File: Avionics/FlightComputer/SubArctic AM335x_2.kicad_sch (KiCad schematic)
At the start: 0 parts

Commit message: Ian Goldberg - Finished sheet no. 1 of the beagleboard and am on to sheet no. 2
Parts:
- added C34: 100uF,10V, symbol Device:C
- added C35, C36: 100nF,16V, symbol Device:C
- added FB7: 150R,800mA, symbol Device:L
- added R37: 0R,5%, symbol Device:R
- added R52, R53: 10K,1%, symbol Device:R
- added U5: ~, symbol SubArctic AM335x:TPS2051BDGNR
- added U6, U8: ~, symbol SubArctic AM335x:TPD4S012DRYR
- added U7: ~, symbol SubArctic AM335x:UB11123-4H9-4F
- added U9: ~, symbol SubArctic AM335x:UX60SC-MB-5ST
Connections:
- new net: U8. (VBUS), U9. (VB) (x3)
- new net: C35.1, FB7.1, R37.2, U5. (PAD), U6. (VBUS)
- new net: FB7.2, U7. (VBUS)
- new net: R53.1, U5. (PAD)
- new net: U6. (VBUS), U7. (VBUS) (x2)
- new net DGND: C34.2, C35.2, C36.2, R53.2, U5. (PAD), U6. (VBUS), U7. (VBUS), U8. (VBUS), U9. (VB)
- new net GNDPWR: U7. (VBUS), U9. (VB)
- new net SYS_5V: C34.1, U5. (PAD)
- new net USB1_OCn: R52.2, U5. (PAD)
- new net USB_DC: C36.1, U8. (VBUS), U9. (VB)
- new net VDD_3V3A: R52.1
- no-connect marks 0 -> 3

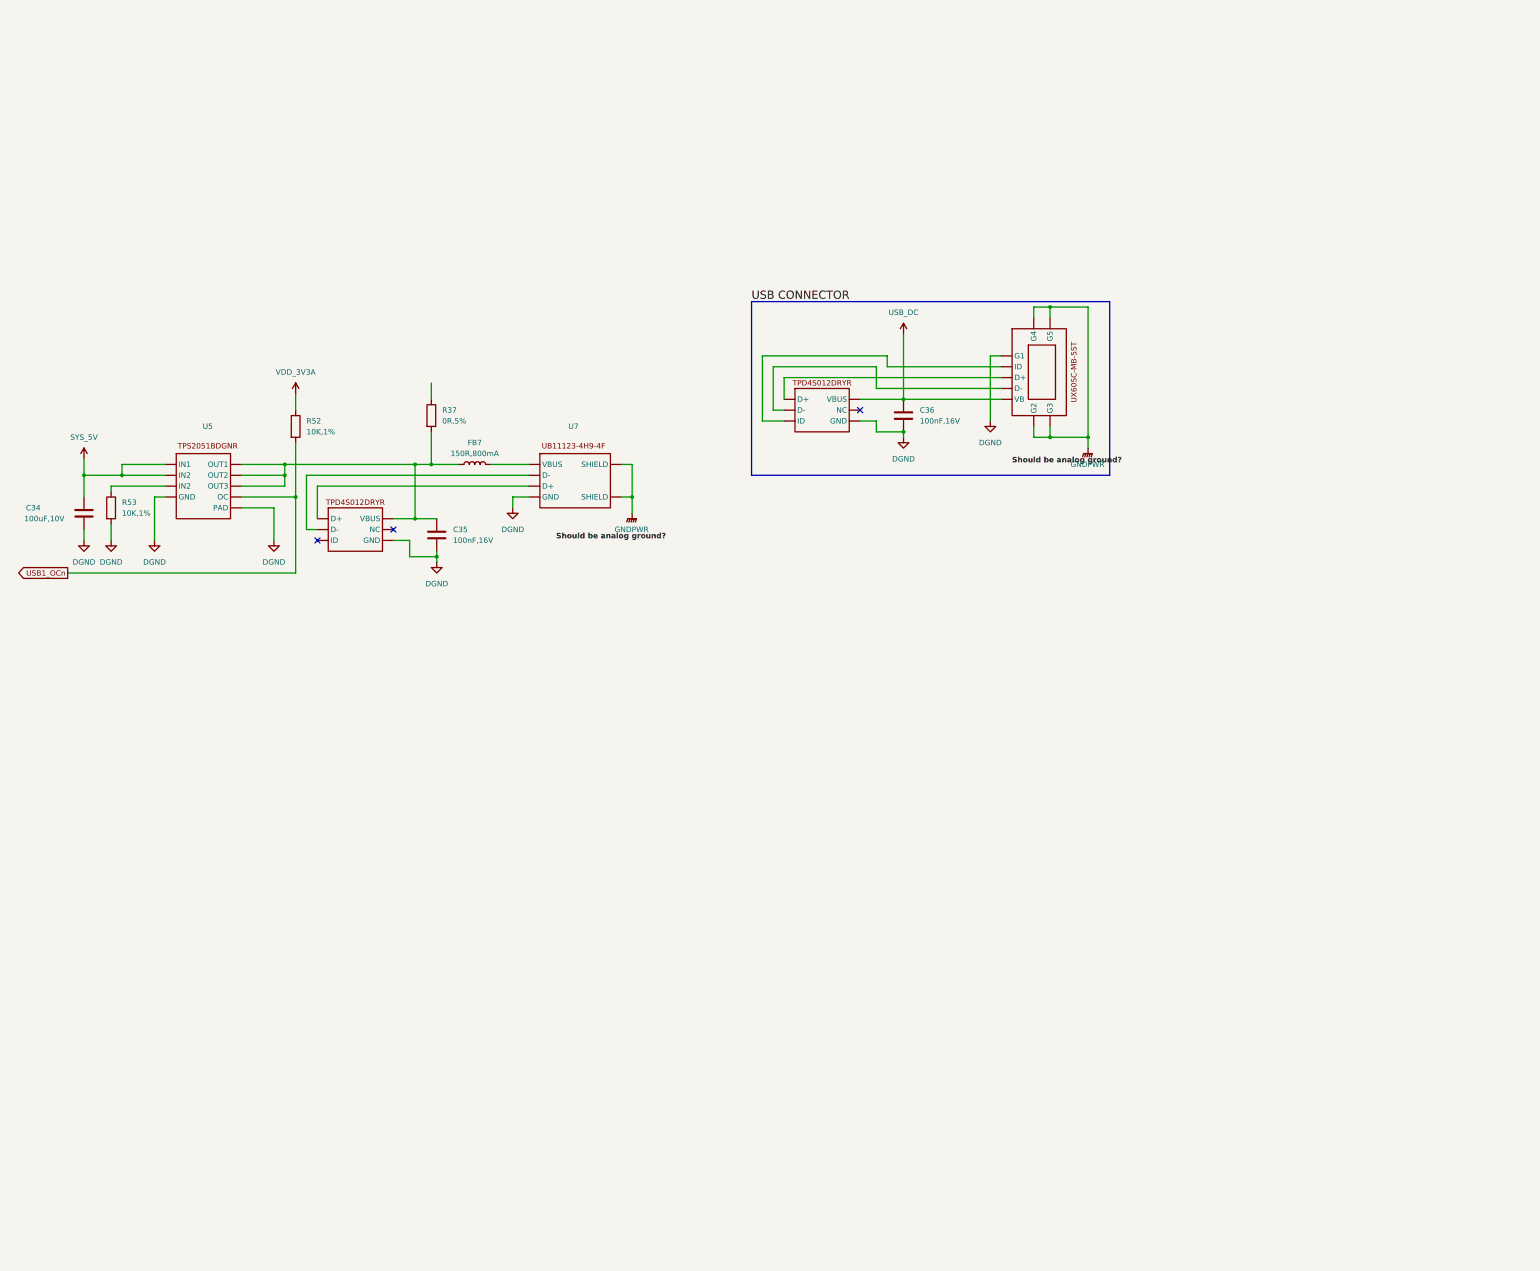
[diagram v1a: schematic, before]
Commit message: Ian Goldberg - Finished the second pin diagram for the SubArctic AM335x chip - only one more to go after this one.
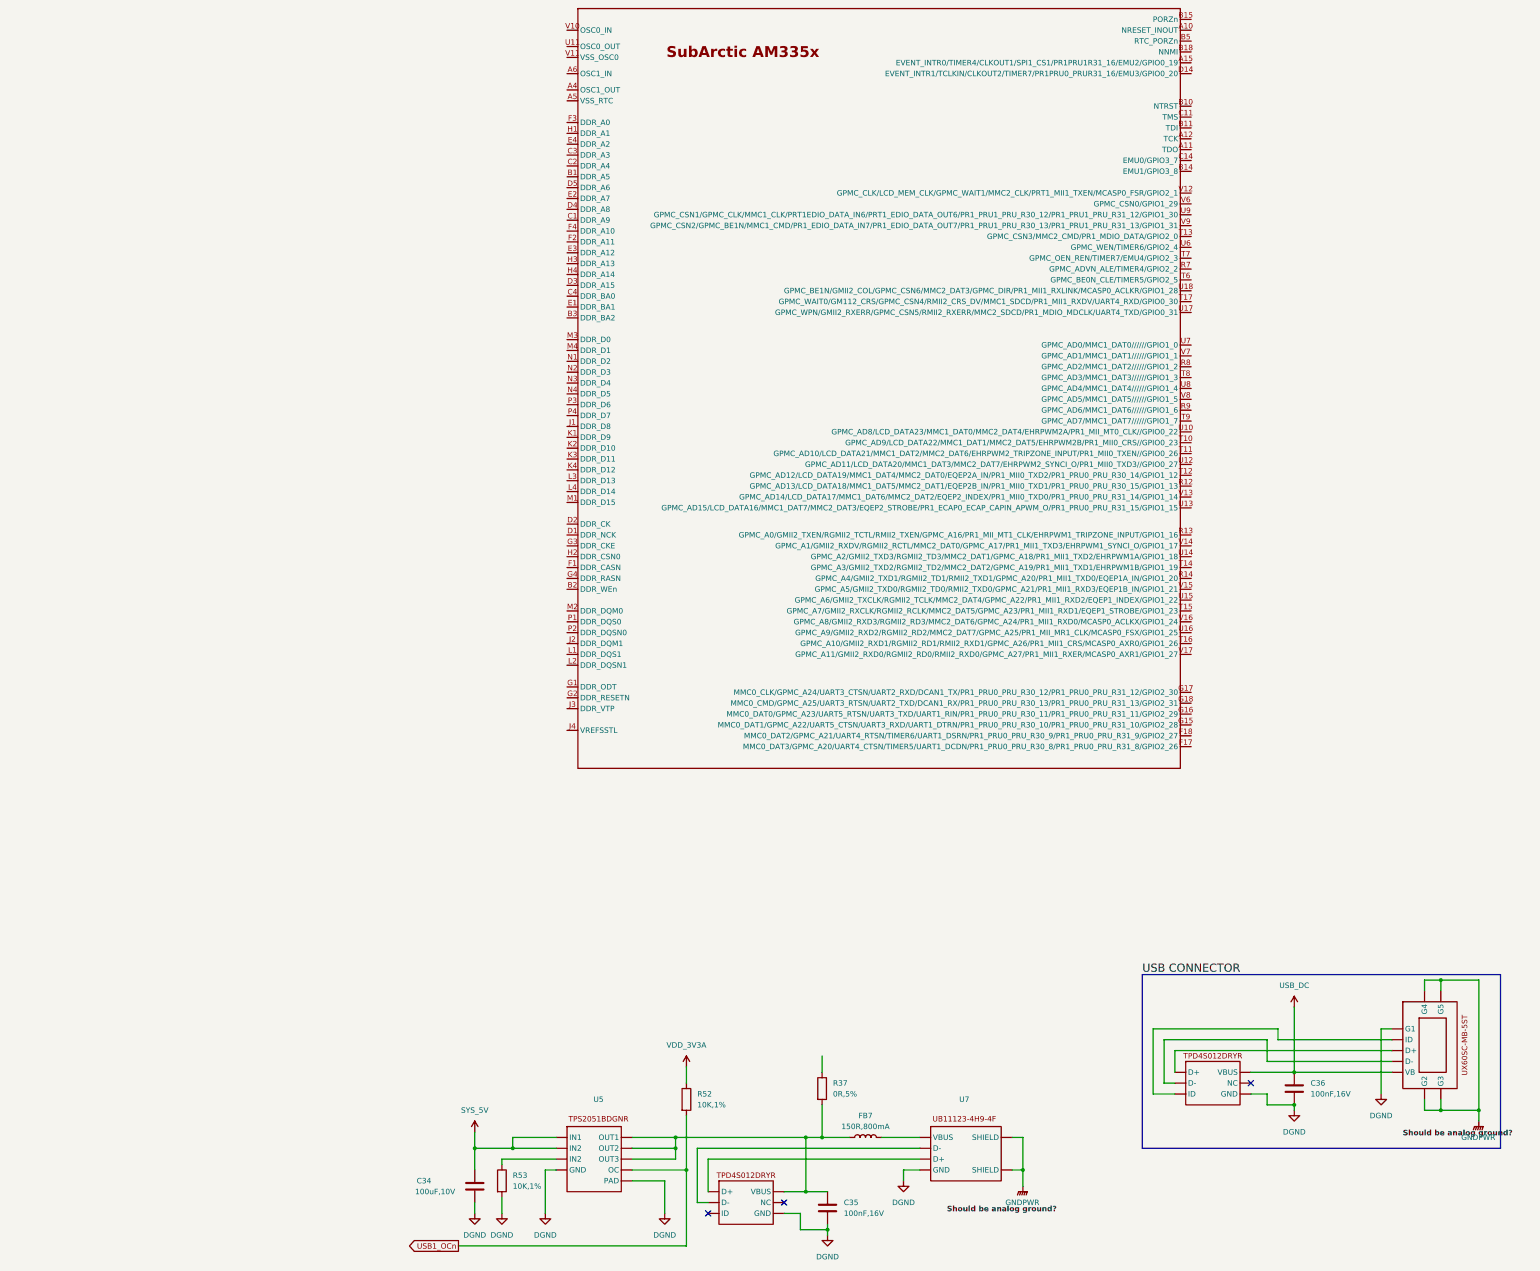
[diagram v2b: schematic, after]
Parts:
- added SubArcticAM335X2: ~, symbol SubArctic AM335x:SubArctic_AM335x_2
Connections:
- new net: U8. (VBUS), U9. (VB) (x3)
- new net: U6. (VBUS), U7. (VBUS) (x2)
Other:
- moved on the sheet: C34, C35, C36, FB7, R37, R52, R53, U5, U7

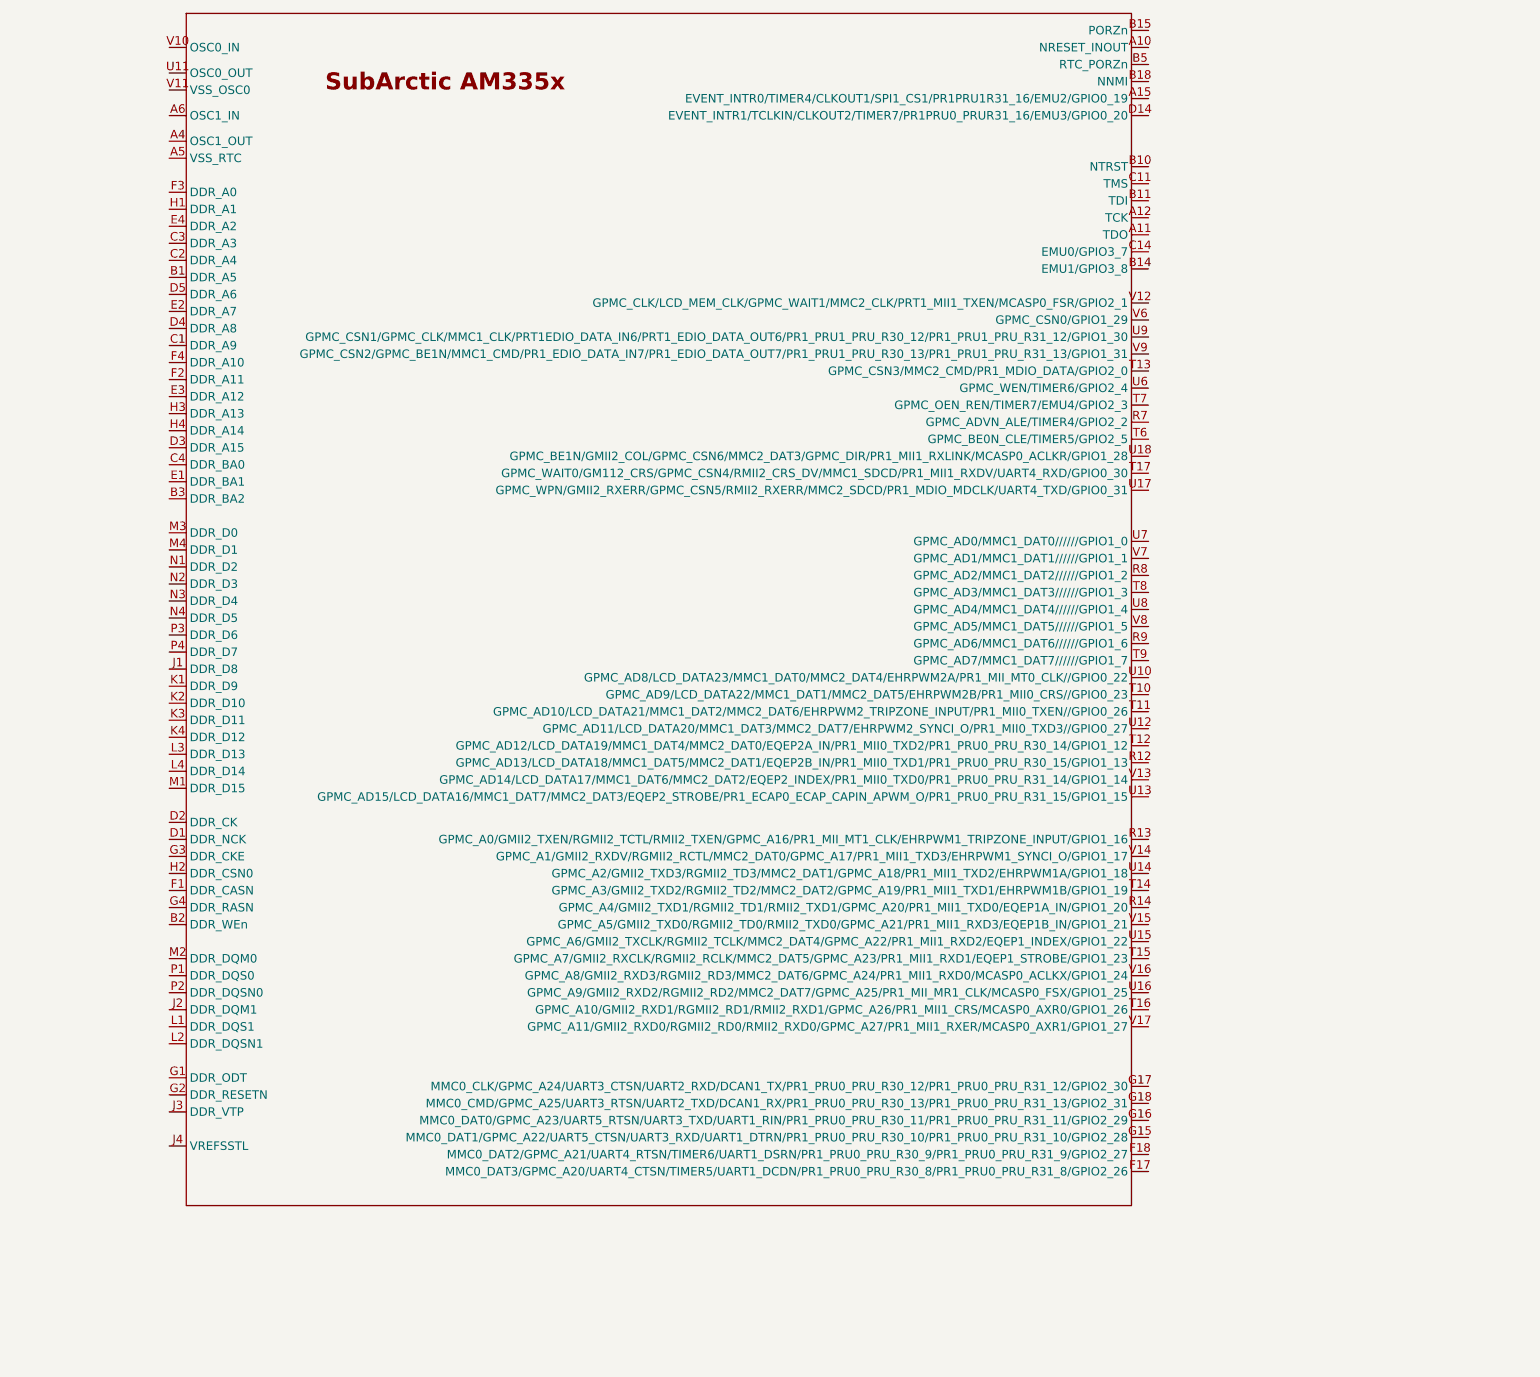
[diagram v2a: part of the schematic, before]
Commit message: Ian Goldberg - Made some tricial changes to the second SubArctic pinout - should have corrected any errors in the pin labeling
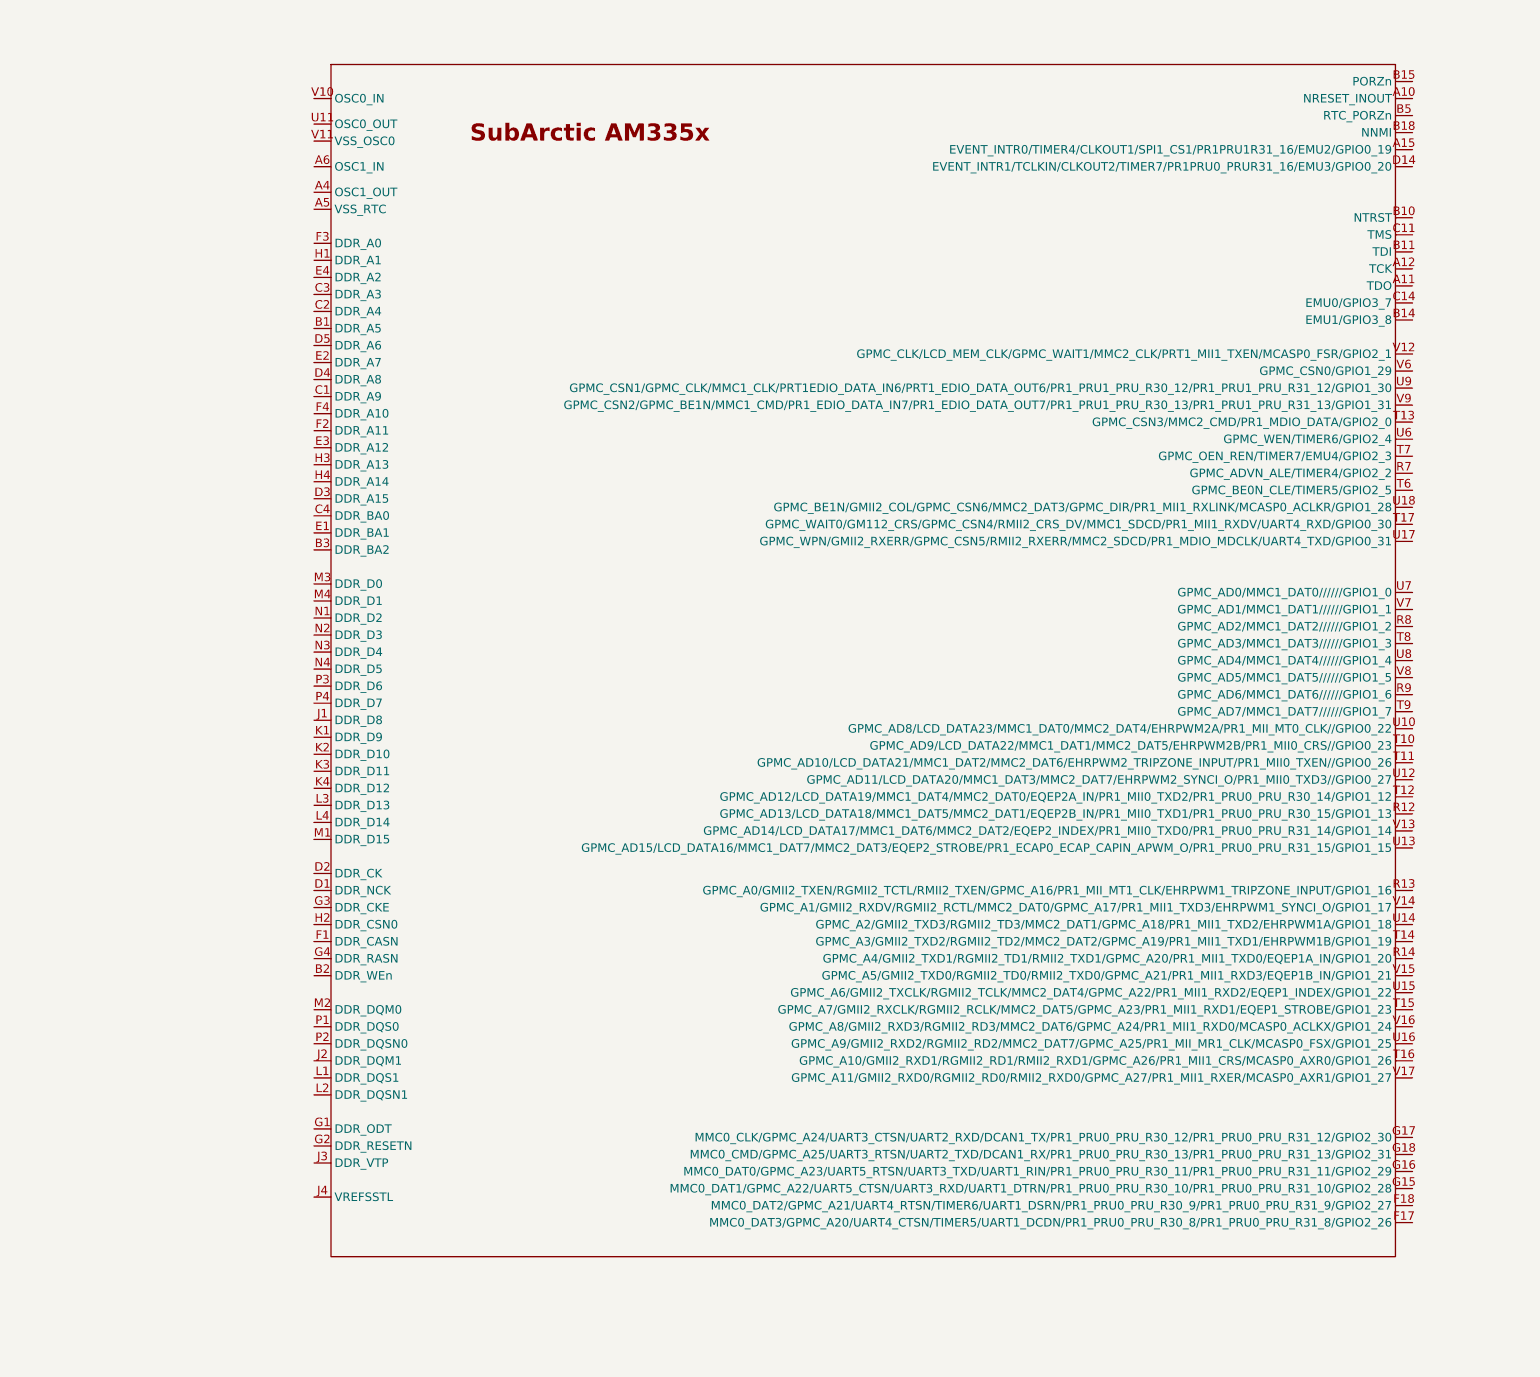
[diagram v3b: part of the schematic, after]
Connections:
- new net: U8. (VBUS), U9. (VB) (x3)
- new net: U6. (VBUS), U7. (VBUS) (x2)
